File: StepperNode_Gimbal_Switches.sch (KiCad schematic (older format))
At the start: 0 parts

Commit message: Added Sheets for Gimbal, Pusher Interlock and Accels
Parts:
- added P?: CONN_01X02_2XMNT, symbol CONN_01X02_2XMNT
- added R? (x2): R, symbol R
- added U? (x2): 74HC14_SCHMITT, symbol 74HC14_SCHMITT
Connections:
- net labels added: GIM1_EXTEND, GIM1_RETRACT, GIM2_EXTEND, GIM2_RETRACT, GIM3_EXTEND, GIM3_RETRACT, GIM4_EXTEND, GIM4_RETRACT, GIMBAL1_SW_EXT, GIMBAL1_SW_RET, GIMBAL2_SW_EXT, GIMBAL2_SW_RET, GIMBAL3_SW_EXT, GIMBAL3_SW_RET, GIMBAL4_SW_EXT, GIMBAL4_SW_RET, GNDD
- wire segments 0 -> 19
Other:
- note added: "Original Author: SafetyLok"
- note added: "rLoop - Stepper Node\nGimbal Switch Interface\n"
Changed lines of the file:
@@
 EELAYER 25 0
 EELAYER END
-$Descr A4 11693 8268
+$Descr A3 16535 11693
 encoding utf-8
-Sheet 1 11
-Title ""
+Sheet 7 12
+Title "Gimbal Switch Interface"
 Date ""
-Rev ""
+Rev "1"
 Comp ""
 Comment1 ""
@@
 Comment4 ""
 $EndDescr
+Text Notes 11850 10350 0    118  ~ 0
+rLoop - Stepper Node\nGimbal Switch Interface\n
+Text Notes 11900 10500 0    60   ~ 0
+Original Author: SafetyLok
+$Comp
+L CONN_01X02_2XMNT P?
+U 1 1 5753C2F3
+P 5600 1600
+F 0 "P?" H 5600 1750 50  0000 C CNN
+F 1 "CONN_01X02_2XMNT" V 5700 1600 50  0000 C CNN
+F 2 "" H 5600 1600 50  0000 C CNN
+F 3 "" H 5600 1600 50  0000 C CNN
+	1    5600 1600
+	1    0    0    -1
+$EndComp
+$Comp
+L 74HC14_SCHMITT U?
+U 1 1 5753C359
+P 2500 3850
+F 0 "U?" H 2800 3800 50  0000 C CNN
+F 1 "74HC14_SCHMITT" H 2800 4750 50  0000 C CNN
+F 2 "" H 2500 3850 50  0000 C CNN
+F 3 "" H 2500 3850 50  0000 C CNN
+	1    2500 3850
+	-1   0    0    -1
+$EndComp
+$Comp
+L R R?
+U 1 1 5753C3EE
+P 4550 1850
+F 0 "R?" V 4630 1850 50  0000 C CNN
+F 1 "R" V 4550 1850 50  0000 C CNN
+F 2 "" V 4480 1850 50  0000 C CNN
+F 3 "" H 4550 1850 50  0000 C CNN
+	1    4550 1850
+	1    0    0    -1
+$EndComp
+$Comp
+L R R?
+U 1 1 5753C447
+P 4550 2150
+F 0 "R?" V 4630 2150 50  0000 C CNN
+F 1 "R" V 4550 2150 50  0000 C CNN
+F 2 "" V 4480 2150 50  0000 C CNN
+F 3 "" H 4550 2150 50  0000 C CNN
+	1    4550 2150
+	1    0    0    -1
+$EndComp
+$Comp
+L GNDD #PWR?
+U 1 1 5753C453
+P 4550 2300
+F 0 "#PWR?" H 4550 2050 50  0001 C CNN
+F 1 "GNDD" H 4550 2150 50  0000 C CNN
+F 2 "" H 4550 2300 50  0000 C CNN
+F 3 "" H 4550 2300 50  0000 C CNN
+	1    4550 2300
+	1    0    0    -1
+$EndComp
+Wire Wire Line
+	5400 1650 4550 1650
+Wire Wire Line
+	4550 1650 4550 1700
+Wire Wire Line
+	4550 2000 3400 2000
+Text Label 3550 2000 0    60   ~ 0
+GIM1_RETRACT
+Text HLabel 1400 3200 0    60   Output ~ 0
+GIMBAL1_SW_RET
+Wire Wire Line
+	1400 3200 1750 3200
+Text HLabel 1400 3300 0    60   Output ~ 0
+GIMBAL1_SW_EXT
+Wire Wire Line
+	1400 3300 1750 3300
+Text HLabel 1400 3400 0    60   Output ~ 0
+GIMBAL2_SW_RET
+Wire Wire Line
+	1400 3400 1750 3400
+Text HLabel 1400 3500 0    60   Output ~ 0
+GIMBAL2_SW_EXT
+Wire Wire Line
+	1400 3500 1750 3500
+$Comp
+L 74HC14_SCHMITT U?
+U 1 1 57547E7D
+P 2500 5100
+F 0 "U?" H 2800 5050 50  0000 C CNN
+F 1 "74HC14_SCHMITT" H 2800 6000 50  0000 C CNN
+F 2 "" H 2500 5100 50  0000 C CNN
+F 3 "" H 2500 5100 50  0000 C CNN
+	1    2500 5100
+	-1   0    0    -1
+$EndComp
+Text HLabel 1400 4450 0    60   Output ~ 0
+GIMBAL3_SW_RET
+Wire Wire Line
+	1400 4450 1750 4450
+Text HLabel 1400 4550 0    60   Output ~ 0
+GIMBAL3_SW_EXT
+Wire Wire Line
+	1400 4550 1750 4550
+Text HLabel 1400 4650 0    60   Output ~ 0
+GIMBAL4_SW_RET
+Wire Wire Line
+	1400 4650 1750 4650
+Text HLabel 1400 4750 0    60   Output ~ 0
+GIMBAL4_SW_EXT
+Wire Wire Line
+	1400 4750 1750 4750
+Wire Wire Line
+	2700 3200 3800 3200
+Text Label 2900 3200 0    60   ~ 0
+GIM1_RETRACT
+Wire Wire Line
+	2700 3300 3800 3300
+Text Label 2900 3300 0    60   ~ 0
+GIM1_EXTEND
+Wire Wire Line
+	2700 3400 3800 3400
+Text Label 2900 3400 0    60   ~ 0
+GIM2_RETRACT
+Wire Wire Line
+	2700 3500 3800 3500
+Text Label 2900 3500 0    60   ~ 0
+GIM2_EXTEND
+Wire Wire Line
+	2700 4450 3800 4450
+Text Label 2900 4450 0    60   ~ 0
+GIM3_RETRACT
+Wire Wire Line
+	2700 4550 3800 4550
+Text Label 2900 4550 0    60   ~ 0
+GIM3_EXTEND
+Wire Wire Line
+	2700 4650 3800 4650
+Text Label 2900 4650 0    60   ~ 0
+GIM4_RETRACT
+Wire Wire Line
+	2700 4750 3800 4750
+Text Label 2900 4750 0    60   ~ 0
+GIM4_EXTEND
 $EndSCHEMATC

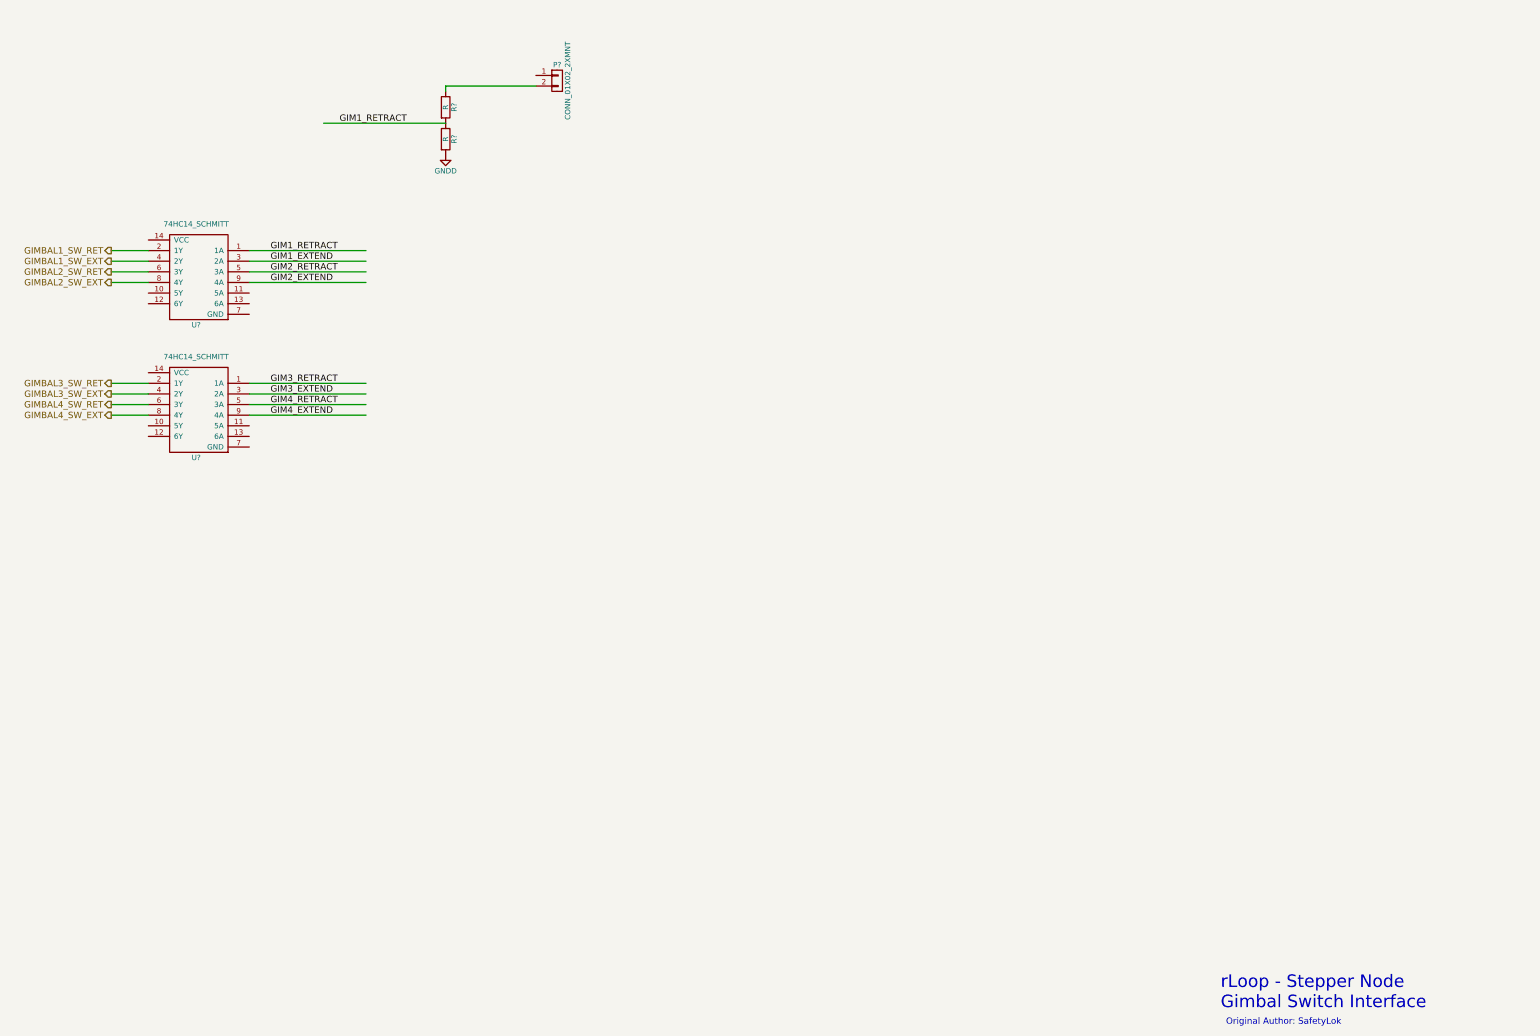
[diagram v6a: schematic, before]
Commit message: Update Gimbal Switch Interface Block
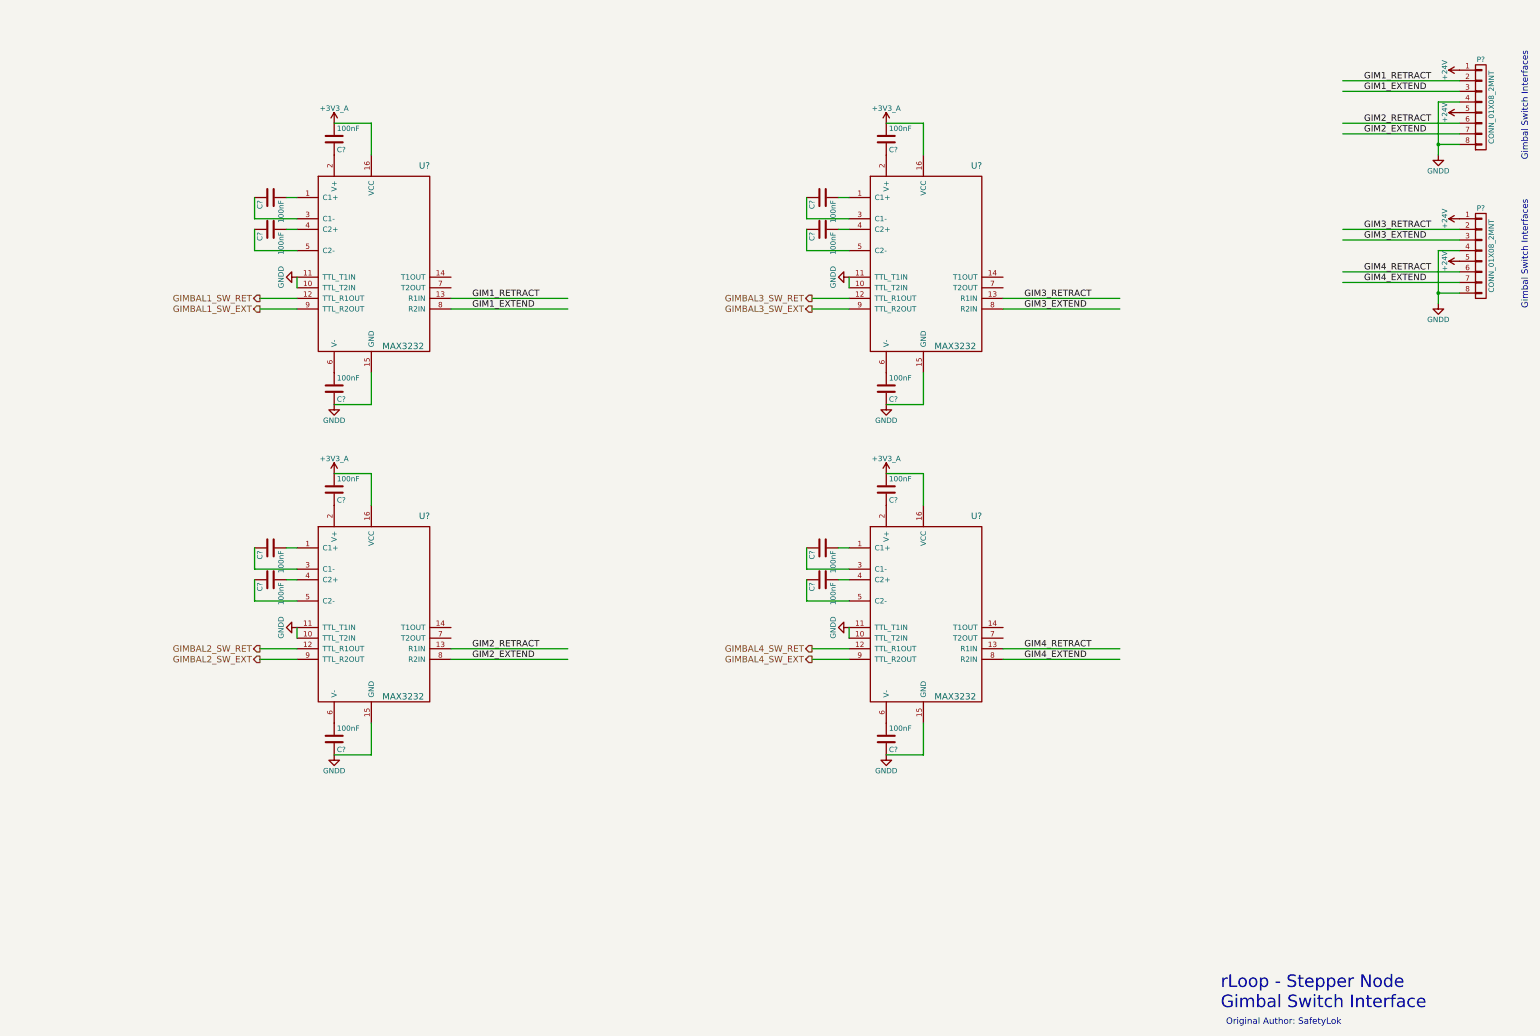
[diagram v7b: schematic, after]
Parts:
- removed P?: CONN_01X02_2XMNT, symbol CONN_01X02_2XMNT
- removed R? (x2): R, symbol R
- removed U? (x2): 74HC14_SCHMITT, symbol 74HC14_SCHMITT
- added C? (x16): 100nF, symbol C
- added P? (x2): CONN_01X08_2MNT, symbol CONN_01X08_2MNT
- added U? (x4): MAX3232, symbol MAX3232
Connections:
- net labels added: +24V, +3V3_A
- wire segments 19 -> 74
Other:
- note added: "Gimbal Switch Interfaces"
